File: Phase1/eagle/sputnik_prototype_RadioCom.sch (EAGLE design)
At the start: 74 parts, among them X2 332-22, Y1 32MHz

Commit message: Lots of OCD cleanup on schematic, bringing up to PSAS standards. Fixed lack of bypass cap on SPI flash, changed SPI flash KW0x pins to SPI1 which weren't before (?), removed DIO1 and DIO0 from GPIO bus, made debug connector, added OreSat v0.3 card outline, roughly positioned connectors, and ran and fixed ERC errors. STILL ERC ERRORS LEFT, specifically the RF_RESET or SOMETHING line. In general: nice work guys! I didn't even hate it.
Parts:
- removed JP1: (no value), psas_c3_team05:PINHD-1X2
- added C42: 100nF, rcl_custom:C-EU0603-B-NOSILK
- added JP2: (no value), pinhead:PINHD-1X12
- added TP10, TP11, TP12, TP13, TP16, TP17, TP9: TPSPAD1-13, testpad:TPSPAD1-13
- C16, C18, C20, C21: value 0.01uF -> 10nF
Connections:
- net GPIO12 renamed PTE16
- net GPIO13 renamed PTE17
- net GPIO14 renamed PTE18
- net GPIO15 renamed PTE19
- net GPIO2 renamed PTB2
- net GPIO3 renamed PTB17
- net N$29 renamed VR_PA
- net PTA0 renamed SWD_CLK
- net PTA3 renamed SWD_DIO
- removed net GPIO0: KW0X.PTB0, X2-1.S
- removed net GPIO1: KW0X.PTB1, X2-2.S
- removed net GPIO10: KW0X.PTE2, X2-11.S
- removed net GPIO11: KW0X.PTE3, X2-12.S
- removed net GPIO16: KW0X.PTE30, X2-17.S
- removed net GPIO4: KW0X.PTC1, X2-5.S
- removed net GPIO5: KW0X.PTC2, X2-6.S
- removed net GPIO6: KW0X.PTC3, X2-7.S
- removed net GPIO7: KW0X.PTC4, X2-8.S
- removed net GPIO8: KW0X.PTC5, X2-9.S
- removed net GPIO9: KW0X.PTC6, X2-10.S
- removed net N$11: C26.1, C27.1, C28.2, C29.2, C39.1, KW0X.VDD, KW0X.VDD2, KW0X.VDDA, KW0X.VREFH, U$8.VOUT
- removed net N$12: KW0X.PTD6, TP4.PP, U$1.DO
- removed net N$14: KW0X.PTD5, TP3.PP, U$1.CLK
- removed net N$15: KW0X.PTD7, TP5.PP, U$1.DI
- removed net N$23: KW0X.PTD0, TP1.PP, U$1.!HOLD
- removed net N$26: KW0X.PTE0, U$1.!WP
- removed net N$28: KW0X.PTD4, TP2.PP, U$1.!CS
- removed net PE0/UART0RX: KW0X.PTA2, TP7.PP, X2-18.S
- removed net PE1/UART0TX: KW0X.PTA1, TP6.PP, X2-19.S
- removed net PE3: J1.SRST, KW0X.PTA20/!RESET, TP8.PP, X2-20.S
- removed net RF_RESET: X2-21.S
- new net !CS: KW0X.PTD4, TP1.PP, U$1.!CS
- new net !HOLD: KW0X.PTE0, TP10.PP, U$1.!HOLD
- new net !RESET: J1.SRST, KW0X.PTA20/!RESET, TP8.PP
- new net !WP: KW0X.PTE1, TP5.PP, U$1.!WP
- new net DIO0: KW0X.PTE2, TP16.PP
- new net DIO1: KW0X.PTE3, TP17.PP
- new net MISO: KW0X.PTD6, TP3.PP, U$1.DO
- new net MOSI: KW0X.PTD7, TP4.PP, U$1.DI
- new net N$3: KW0X.DIO2, TP11.PP
- new net N$4: TP9.PP, U$9.PG
- new net N$5: KW0X.DIO3, TP12.PP
- new net N$9: KW0X.DIO4, TP13.PP
- new net PTC1: JP2.3, KW0X.PTC1, X2-5.S
- new net PTC2: JP2.4, KW0X.PTC2, X2-6.S
- new net PTC3: JP2.5, KW0X.PTC3, X2-7.S
- new net PTC4: JP2.6, KW0X.PTC4, X2-8.S
- new net PTC5: JP2.7, KW0X.PTC5, X2-9.S
- new net PTC6: JP2.8, KW0X.PTC6, X2-10.S
- new net PTC7: JP2.9, KW0X.PTC7, X2-11.S
- new net PTD0: KW0X.PTD0, X2-12.S
- new net PTE30: KW0X.PTE30
- new net SCLK: KW0X.PTD5, TP2.PP, U$1.CLK
- new net UART0_RX: JP2.10, KW0X.PTA1, TP6.PP, X2-19.S, X2-20.S
- new net UART0_TX: JP2.11, KW0X.PTA2, TP7.PP, X2-17.S, X2-18.S
- net 3.3V: now also C26.1, C27.1, C28.2, C29.2, C39.1, C42.2, JP2.2, KW0X.VDD, KW0X.VDD2, KW0X.VDDA, KW0X.VREFH, U$1.VDD, U$8.VOUT
- net GND: now also C42.1, JP2.12, X2-21.S, X2-22.S; no longer JP1.2, U$9.PG
- net LNA_EN: now also KW0X.PTB0; no longer KW0X.PTC7
- net PA_EN: now also KW0X.PTB1; no longer KW0X.PTE1
- net V+: now also JP2.1, X2-1.S, X2-2.S; no longer JP1.1, U$1.VDD, X2-22.S
- net VBIAS: now also LNA.NC
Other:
- note added: "DO YOU REALLY NEED !WP and !HOLD?"
- note added: "DOES !RESET NEED A PULL-UP?!"
- note added: "Debug interface"
- note added: "FIXME!!!!"
- note added: "MCX to 70 cm Antenna"
- note added: "NC??"
- note added: "ORESAT BACKPLANE"
- note added: "Placed by access edge"
- note added: "TODO: FIGURE OUT VALUES FOR LNA"
- note added: "WHY IS NC CONNECTED TO VCC?"
- note removed: "All these go to 22 pinout"
- note removed: "Antenna"
- note removed: "KW0x LDO"
- note removed: "Need to figure out values for LNA"
- note removed: "Power Interface"
- note removed: "System Controller"
- note removed: "for VDDA"
- note removed: "for VREFH"
- note removed: "power"
- moved on the sheet: C1, C10, C11, C12, C13, C14, C15, C16, C17, C18, C19, C2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

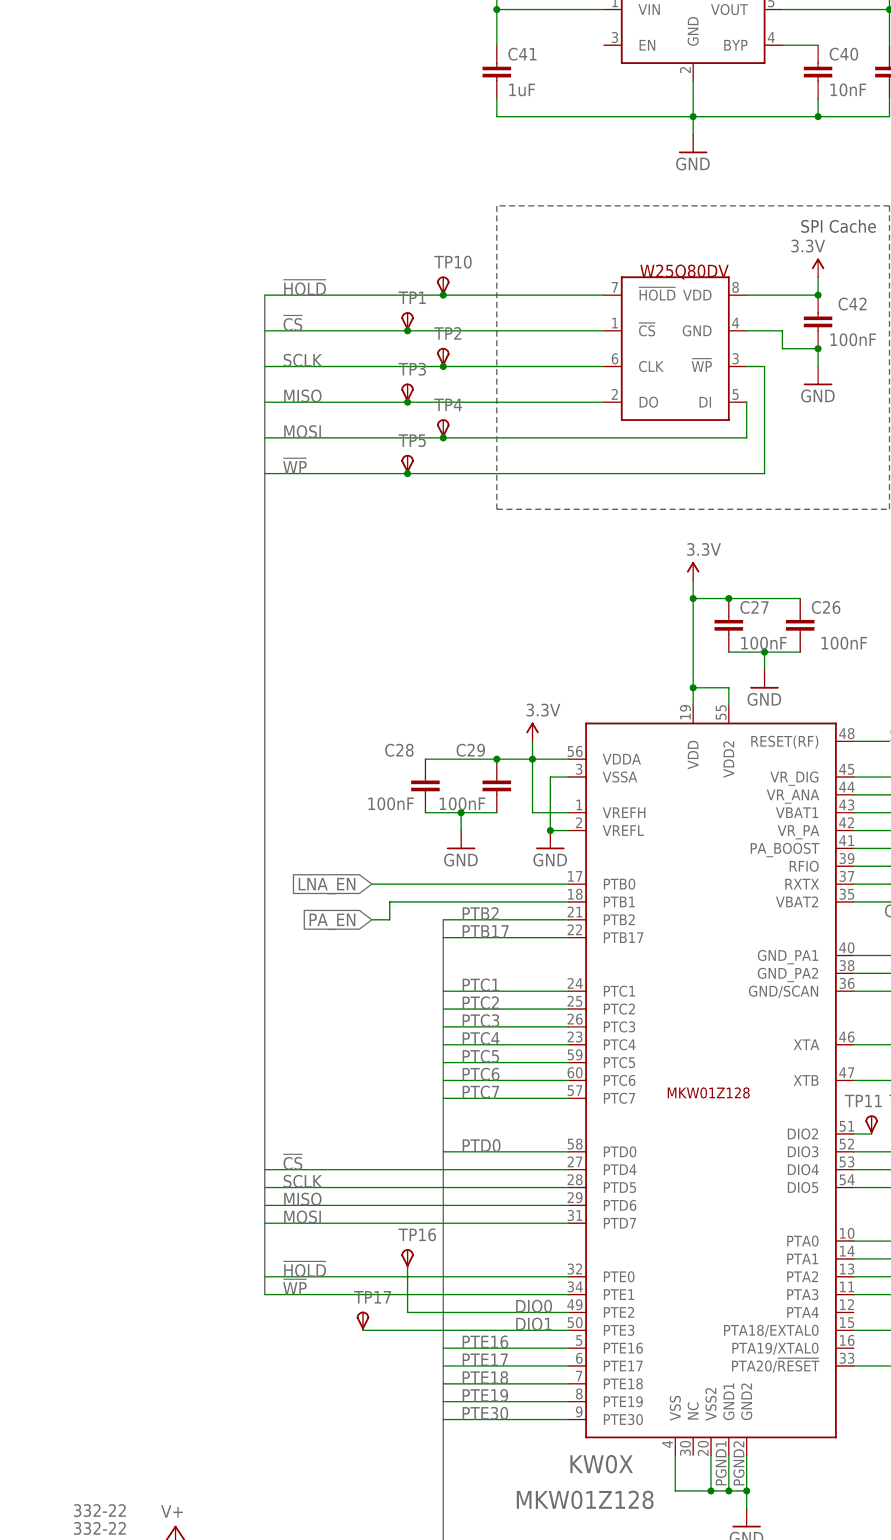
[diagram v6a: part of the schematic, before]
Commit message: Added 44pin symbol and pull-up lines on SPI Cache
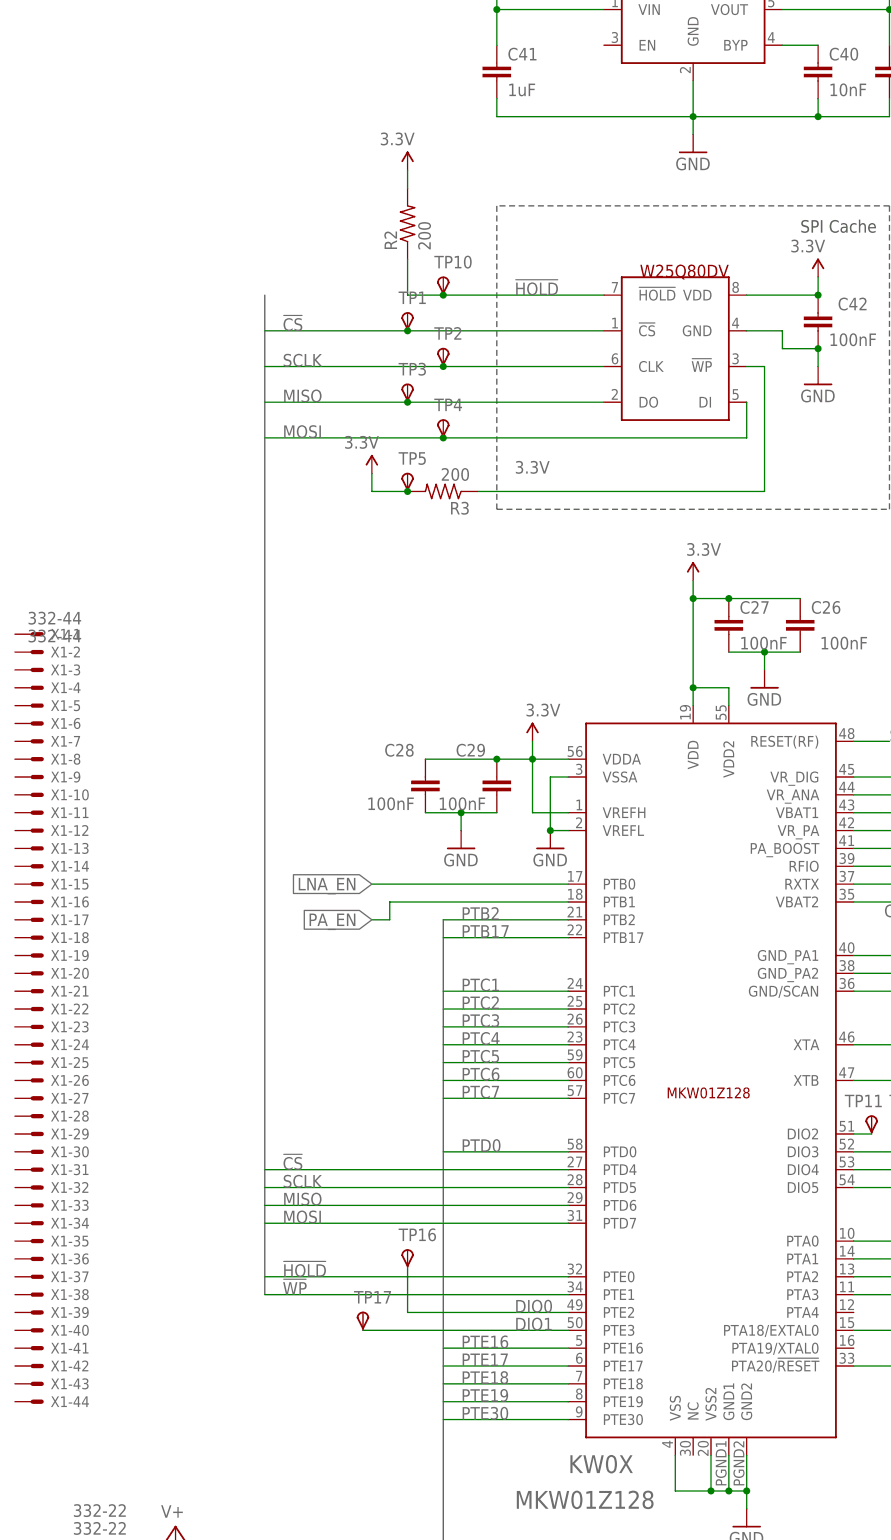
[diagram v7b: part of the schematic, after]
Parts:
- added R2, R3: 200, rcl_custom:R-US_0603-B-NOSILK
- added X1: 332-44, con-garry:332-44
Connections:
- new net N$11: R3.1, U$1.!WP
- net !HOLD: now also R2.1
- net !WP: no longer TP5.PP, U$1.!WP
- net 3.3V: now also R2.2, R3.2, TP5.PP
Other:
- note removed: "DO YOU REALLY NEED !WP and !HOLD?"
- moved on the sheet: TP5

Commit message: Fixed 22x2pinout, added PWR LEDs, fixed some NC issues
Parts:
- removed X2: 332-22, con-garry:332-22
- added LED1, LED2, LED3, LED4, LED5, LED6: (no value), psas_c3_team05:LED-0603
- added R10, R4, R6, R7, R8, R9: 1k, rcl_custom:R-US_0603-B-NOSILK
- added R5: 10k, rcl_custom:R-US_0603-B-NOSILK
- added TP14: TPSPAD1-13, testpad:TPSPAD1-13
- R2, R3: value 200 -> 10k
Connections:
- new net 3.3V1: LED2.A
- new net N$12: R5.1, TP14.PP, U$8.EN
- new net N$14: LED1.K, R4.2
- new net N$15: LED2.K, R6.2
- new net N$20: LED3.K, R7.2
- new net N$22: LED4.K, R8.2
- new net N$26: LED5.K, R9.2
- new net N$28: LED5.A
- new net N$29: LED6.K, R10.2
- new net N$32: LED6.A
- net 3.3V: now also LED4.A
- net GND: now also LNA.NC, R10.1, R4.1, R6.1, R7.1, R8.1, R9.1, X1-21.S, X1-22.S; no longer X2-21.S, X2-22.S
- net PTB17: now also X1-4.S; no longer X2-4.S
- net PTB2: now also X1-3.S; no longer X2-3.S
- net PTC1: now also X1-5.S; no longer X2-5.S
- net PTC2: now also X1-6.S; no longer X2-6.S
- net PTC3: now also X1-7.S; no longer X2-7.S
- net PTC4: now also X1-8.S; no longer X2-8.S
- net PTC5: now also X1-9.S; no longer X2-9.S
- net PTC6: now also X1-10.S; no longer X2-10.S
- net PTC7: now also X1-11.S; no longer X2-11.S
- net PTD0: now also X1-12.S; no longer X2-12.S
- net PTE16: now also X1-13.S; no longer X2-13.S
- net PTE17: now also X1-14.S; no longer X2-14.S
- net PTE18: now also X1-15.S; no longer X2-15.S
- net PTE19: now also X1-16.S; no longer X2-16.S
- net UART0_RX: now also X1-19.S, X1-20.S; no longer X2-19.S, X2-20.S
- net UART0_TX: now also X1-17.S, X1-18.S; no longer X2-17.S, X2-18.S
- net V+: now also LED1.A, R5.2, X1-1.S, X1-2.S; no longer X2-1.S, X2-2.S
- net VBIAS: no longer LNA.NC
- net VPA: now also LED3.A
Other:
- note removed: "NC??"
- note removed: "WHY IS NC CONNECTED TO VCC?"
- moved on the sheet: C36, C39, C40, C41, X1-1, X1-10, X1-11, X1-12, X1-13, X1-14, X1-15, X1-16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
